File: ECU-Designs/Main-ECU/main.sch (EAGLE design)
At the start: 22 parts, among them X1 MINIFIT_5566-4

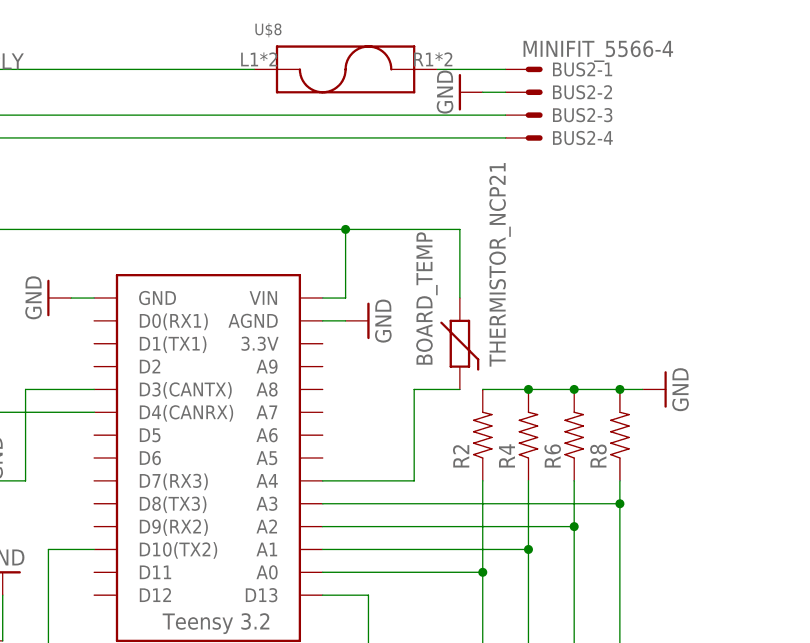
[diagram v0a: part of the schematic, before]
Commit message: Fix main board thermistor, add voltage cutoff to external diagram
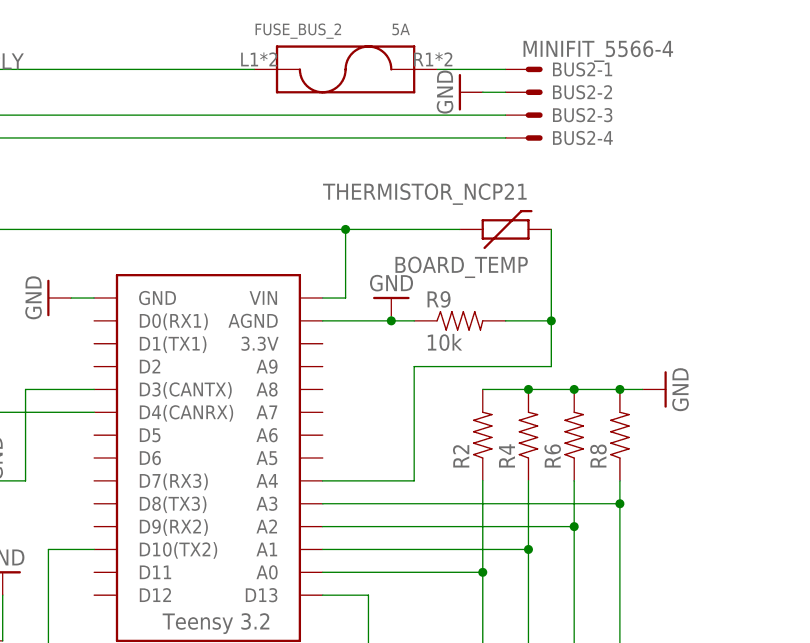
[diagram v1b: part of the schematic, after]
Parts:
- added R9: 10k, HyTechDevices:RESISTOR2010
- FUSE_BUS_2: value (none) -> 5A
- renumbered U$8 to FUSE_BUS_2
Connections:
- net N$12 renamed SHUTDOWN_OUT_READ
- net N$14 renamed 12VSUPPLY_READ
- net N$7 renamed OKHS_READ
- net N$9 renamed BMS_OK_READ
- net GND: now also R9.1
- net N$15: now also R9.2
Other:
- moved on the sheet: BOARD_TEMP
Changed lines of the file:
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@@
 <part name="BUS2" library="HyTechDevices" deviceset="MINIFIT_5566-4" device=""/>
 <part name="FUSE_BUS_1" library="HyTechDevices" deviceset="FUSE_HOLDER" device="" value="5A"/>
-<part name="U$8" library="HyTechDevices" deviceset="FUSE_HOLDER" device=""/>
+<part name="FUSE_BUS_2" library="HyTechDevices" deviceset="FUSE_HOLDER" device="" value="5A"/>
 <part name="GND2" library="HyTechSymbols" deviceset="GND" device=""/>
 <part name="GND15" library="HyTechSymbols" deviceset="GND" device=""/>
@@
 <part name="R8" library="HyTechDevices" deviceset="RESISTOR" device="2010"/>
 <part name="BOARD_TEMP" library="HyTechDevices" deviceset="THERMISTOR_NCP21" device=""/>
+<part name="R9" library="HyTechDevices" deviceset="RESISTOR" device="2010" value="10k"/>
 </parts>
 <sheets>
@@
 <instance part="U$3" gate="G$1" x="73.66" y="38.1"/>
 <instance part="GND10" gate="1" x="66.04" y="76.2" rot="R270"/>
-<instance part="GND11" gate="1" x="101.6" y="73.66" rot="R90"/>
+<instance part="GND11" gate="1" x="104.14" y="76.2" rot="R180"/>
 <instance part="CAN_TRANSCEIVER" gate="G$1" x="50.8" y="63.5" rot="R180"/>
 <instance part="GND12" gate="1" x="58.42" y="58.42" rot="R90"/>
@@
 <instance part="BUS2" gate="-4" x="119.38" y="93.98"/>
 <instance part="FUSE_BUS_1" gate="G$1" x="5.08" y="99.06"/>
-<instance part="U$8" gate="G$1" x="99.06" y="99.06"/>
+<instance part="FUSE_BUS_2" gate="G$1" x="99.06" y="99.06"/>
 <instance part="GND2" gate="1" x="-7.62" y="81.28" rot="R90"/>
 <instance part="GND15" gate="1" x="-7.62" y="99.06" rot="R90"/>
@@
 <instance part="R7" gate="G$1" x="129.54" y="30.48" rot="R90"/>
 <instance part="R8" gate="G$1" x="129.54" y="60.96" rot="R90"/>
-<instance part="BOARD_TEMP" gate="G$1" x="111.76" y="71.12" rot="R90"/>
+<instance part="BOARD_TEMP" gate="G$1" x="116.84" y="83.82" rot="R180"/>
+<instance part="R9" gate="G$1" x="111.76" y="73.66"/>
 </instances>
 <busses>
@@
 <pinref part="U$3" gate="G$1" pin="AGND"/>
 <pinref part="GND11" gate="1" pin="GND"/>
-<wire x1="99.06" y1="73.66" x2="96.52" y2="73.66" width="0.1524" layer="91"/>
+<wire x1="104.14" y1="73.66" x2="96.52" y2="73.66" width="0.1524" layer="91"/>
+<pinref part="R9" gate="G$1" pin="1"/>
+<wire x1="104.14" y1="73.66" x2="106.68" y2="73.66" width="0.1524" layer="91"/>
+<junction x="104.14" y="73.66"/>
 </segment>
 <segment>
@@
 <junction x="58.42" y="83.82"/>
 <pinref part="BOARD_TEMP" gate="G$1" pin="1"/>
-<wire x1="111.76" y1="76.2" x2="111.76" y2="83.82" width="0.1524" layer="91"/>
 <wire x1="111.76" y1="83.82" x2="99.06" y2="83.82" width="0.1524" layer="91"/>
 <junction x="99.06" y="83.82"/>
@@
 <net name="N$11" class="0">
 <segment>
-<pinref part="U$8" gate="G$1" pin="2"/>
+<pinref part="FUSE_BUS_2" gate="G$1" pin="2"/>
 <pinref part="BUS2" gate="-1" pin="S"/>
 <wire x1="109.22" y1="101.6" x2="116.84" y2="101.6" width="0.1524" layer="91"/>
@@
 <pinref part="IMD_SHUTDOWN" gate="G$1" pin="6"/>
 <pinref part="POWER" gate="-1" pin="S"/>
-<pinref part="U$8" gate="G$1" pin="1"/>
+<pinref part="FUSE_BUS_2" gate="G$1" pin="1"/>
 <pinref part="FUSE_BUS_1" gate="G$1" pin="2"/>
 <wire x1="88.9" y1="101.6" x2="17.78" y2="101.6" width="0.1524" layer="91"/>
@@
 </segment>
 </net>
-<net name="N$7" class="0">
+<net name="OKHS_READ" class="0">
 <segment>
 <pinref part="R2" gate="G$1" pin="1"/>
@@
 </segment>
 </net>
-<net name="N$9" class="0">
+<net name="BMS_OK_READ" class="0">
 <segment>
 <pinref part="R3" gate="G$1" pin="2"/>
@@
 </segment>
 </net>
-<net name="N$12" class="0">
+<net name="SHUTDOWN_OUT_READ" class="0">
 <segment>
 <pinref part="R6" gate="G$1" pin="1"/>
@@
 </segment>
 </net>
-<net name="N$14" class="0">
+<net name="12VSUPPLY_READ" class="0">
 <segment>
 <pinref part="R8" gate="G$1" pin="1"/>
@@
 <net name="N$15" class="0">
 <segment>
-<pinref part="BOARD_TEMP" gate="G$1" pin="2"/>
-<wire x1="111.76" y1="66.04" x2="106.68" y2="66.04" width="0.1524" layer="91"/>
-<wire x1="106.68" y1="66.04" x2="106.68" y2="55.88" width="0.1524" layer="91"/>
+<wire x1="106.68" y1="68.58" x2="106.68" y2="55.88" width="0.1524" layer="91"/>
 <pinref part="U$3" gate="G$1" pin="A4"/>
 <wire x1="106.68" y1="55.88" x2="96.52" y2="55.88" width="0.1524" layer="91"/>
-</segment>
-</net>
+<pinref part="R9" gate="G$1" pin="2"/>
+<pinref part="BOARD_TEMP" gate="G$1" pin="2"/>
+<wire x1="116.84" y1="73.66" x2="121.92" y2="73.66" width="0.1524" layer="91"/>
+<wire x1="121.92" y1="73.66" x2="121.92" y2="83.82" width="0.1524" layer="91"/>
+<wire x1="106.68" y1="68.58" x2="121.92" y2="68.58" width="0.1524" layer="91"/>
+<wire x1="121.92" y1="68.58" x2="121.92" y2="73.66" width="0.1524" layer="91"/>
+<junction x="121.92" y="73.66"/>
+</segment>
+</net>

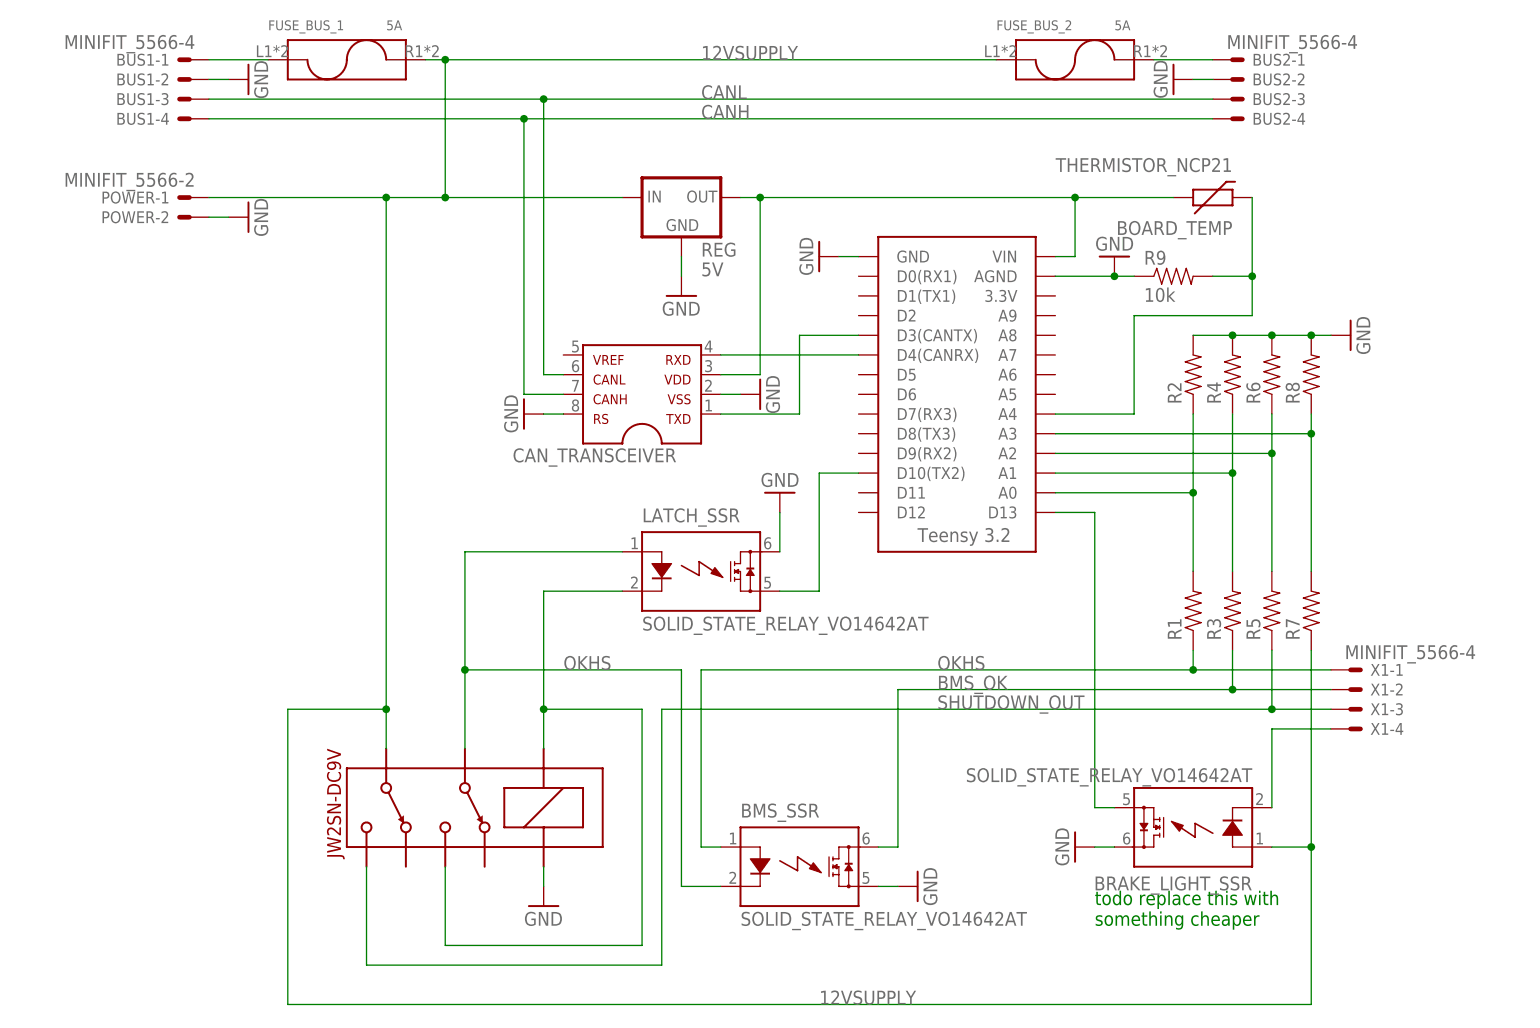
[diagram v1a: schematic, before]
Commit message: Add resistors, fix ssrs on main ecu
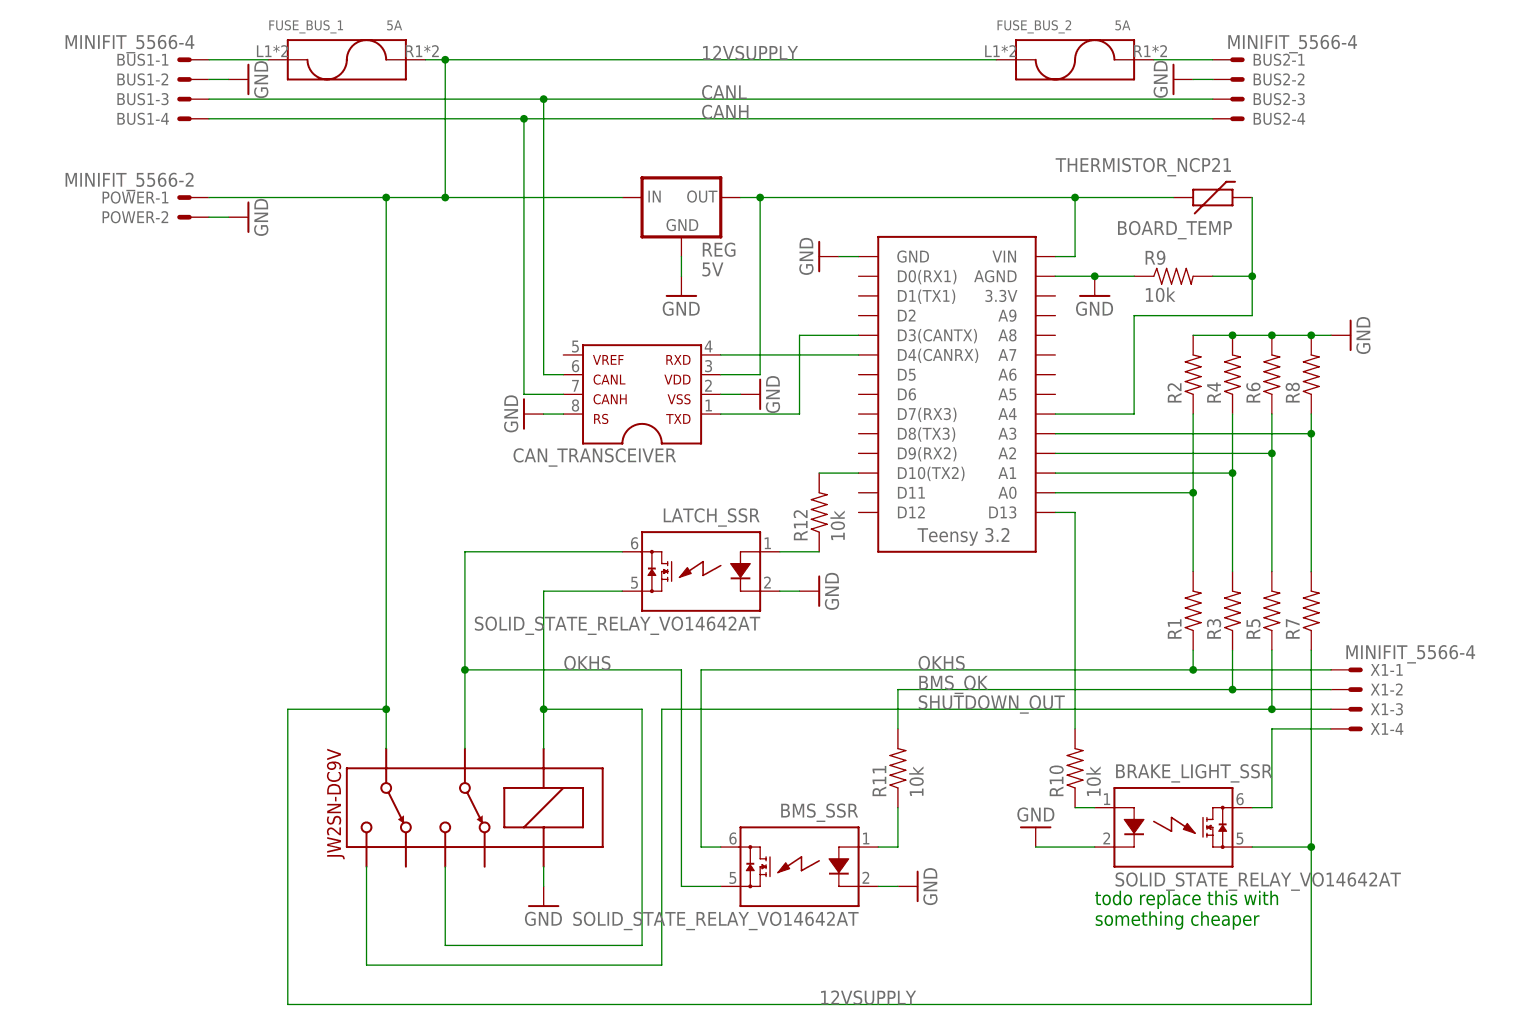
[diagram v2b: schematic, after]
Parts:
- added R10, R11, R12: 10k, HyTechDevices:RESISTOR2010
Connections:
- new net N$12: LATCH_SSR.LED+, R12.1
- new net N$7: BRAKE_LIGHT_SSR.LED+, R10.1
- new net N$9: BMS_SSR.LED+, R11.1
- net 12VSUPPLY: now also BRAKE_LIGHT_SSR.IO2; no longer BRAKE_LIGHT_SSR.LED+
- net BMS_OK: now also R11.2; no longer BMS_SSR.IO1
- net GND: now also BMS_SSR.LED-, BRAKE_LIGHT_SSR.LED-, LATCH_SSR.LED-; no longer BMS_SSR.IO2, BRAKE_LIGHT_SSR.IO1, LATCH_SSR.IO1
- net N$13: now also R10.2; no longer BRAKE_LIGHT_SSR.IO2
- net N$4: now also BRAKE_LIGHT_SSR.IO1; no longer BRAKE_LIGHT_SSR.LED-
- net N$5: now also R12.2; no longer LATCH_SSR.IO2
- net N$6: now also LATCH_SSR.IO2; no longer LATCH_SSR.LED-
- net N$8: now also BMS_SSR.IO1; no longer BMS_SSR.LED+
- net OKHS: now also BMS_SSR.IO2, LATCH_SSR.IO1; no longer BMS_SSR.LED-, LATCH_SSR.LED+
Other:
- moved on the sheet: BRAKE_LIGHT_SSR

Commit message: Finish first version of main ecu board
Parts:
- R1, R10, R11, R12, R2, R3, R4, R5, R6, R7, R8, R9: device HyTechDevices:RESISTOR2010 -> HyTechDevices:RESISTOR0805-RES
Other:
- note removed: "todo replace this with something cheaper"
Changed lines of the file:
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@@
 <part name="BMS_SSR" library="HyTechDevices" deviceset="SOLID_STATE_RELAY" device="_VO14642AT"/>
 <part name="GND3" library="HyTechSymbols" deviceset="GND" device=""/>
-<part name="R1" library="HyTechDevices" deviceset="RESISTOR" device="2010"/>
-<part name="R2" library="HyTechDevices" deviceset="RESISTOR" device="2010"/>
-<part name="R3" library="HyTechDevices" deviceset="RESISTOR" device="2010"/>
-<part name="R4" library="HyTechDevices" deviceset="RESISTOR" device="2010"/>
-<part name="R5" library="HyTechDevices" deviceset="RESISTOR" device="2010"/>
-<part name="R6" library="HyTechDevices" deviceset="RESISTOR" device="2010"/>
+<part name="R1" library="HyTechDevices" deviceset="RESISTOR" device="0805-RES"/>
+<part name="R2" library="HyTechDevices" deviceset="RESISTOR" device="0805-RES"/>
+<part name="R3" library="HyTechDevices" deviceset="RESISTOR" device="0805-RES"/>
+<part name="R4" library="HyTechDevices" deviceset="RESISTOR" device="0805-RES"/>
+<part name="R5" library="HyTechDevices" deviceset="RESISTOR" device="0805-RES"/>
+<part name="R6" library="HyTechDevices" deviceset="RESISTOR" device="0805-RES"/>
 <part name="GND4" library="HyTechSymbols" deviceset="GND" device=""/>
-<part name="R7" library="HyTechDevices" deviceset="RESISTOR" device="2010"/>
-<part name="R8" library="HyTechDevices" deviceset="RESISTOR" device="2010"/>
+<part name="R7" library="HyTechDevices" deviceset="RESISTOR" device="0805-RES"/>
+<part name="R8" library="HyTechDevices" deviceset="RESISTOR" device="0805-RES"/>
 <part name="BOARD_TEMP" library="HyTechDevices" deviceset="THERMISTOR_NCP21" device=""/>
-<part name="R9" library="HyTechDevices" deviceset="RESISTOR" device="2010" value="10k"/>
-<part name="R10" library="HyTechDevices" deviceset="RESISTOR" device="2010" value="10k"/>
-<part name="R11" library="HyTechDevices" deviceset="RESISTOR" device="2010" value="10k"/>
-<part name="R12" library="HyTechDevices" deviceset="RESISTOR" device="2010" value="10k"/>
+<part name="R9" library="HyTechDevices" deviceset="RESISTOR" device="0805-RES" value="10k"/>
+<part name="R10" library="HyTechDevices" deviceset="RESISTOR" device="0805-RES" value="10k"/>
+<part name="R11" library="HyTechDevices" deviceset="RESISTOR" device="0805-RES" value="10k"/>
+<part name="R12" library="HyTechDevices" deviceset="RESISTOR" device="0805-RES" value="10k"/>
 </parts>
 <sheets>
 <sheet>
 <plain>
-<text x="101.6" y="-10.16" size="1.778" layer="91">todo replace this with
-something cheaper</text>
 </plain>
 <instances>
@@
 </schematic>
 </drawing>
-<compatibility>
-<note version="6.3" minversion="6.2.2" severity="warning">
-Since Version 6.2.2 text objects can contain more than one line,
-which will not be processed correctly with this version.
-</note>
-</compatibility>
 </eagle>
